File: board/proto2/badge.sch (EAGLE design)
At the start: 59 parts, among them IC1 TLV62569, J1 5051101092

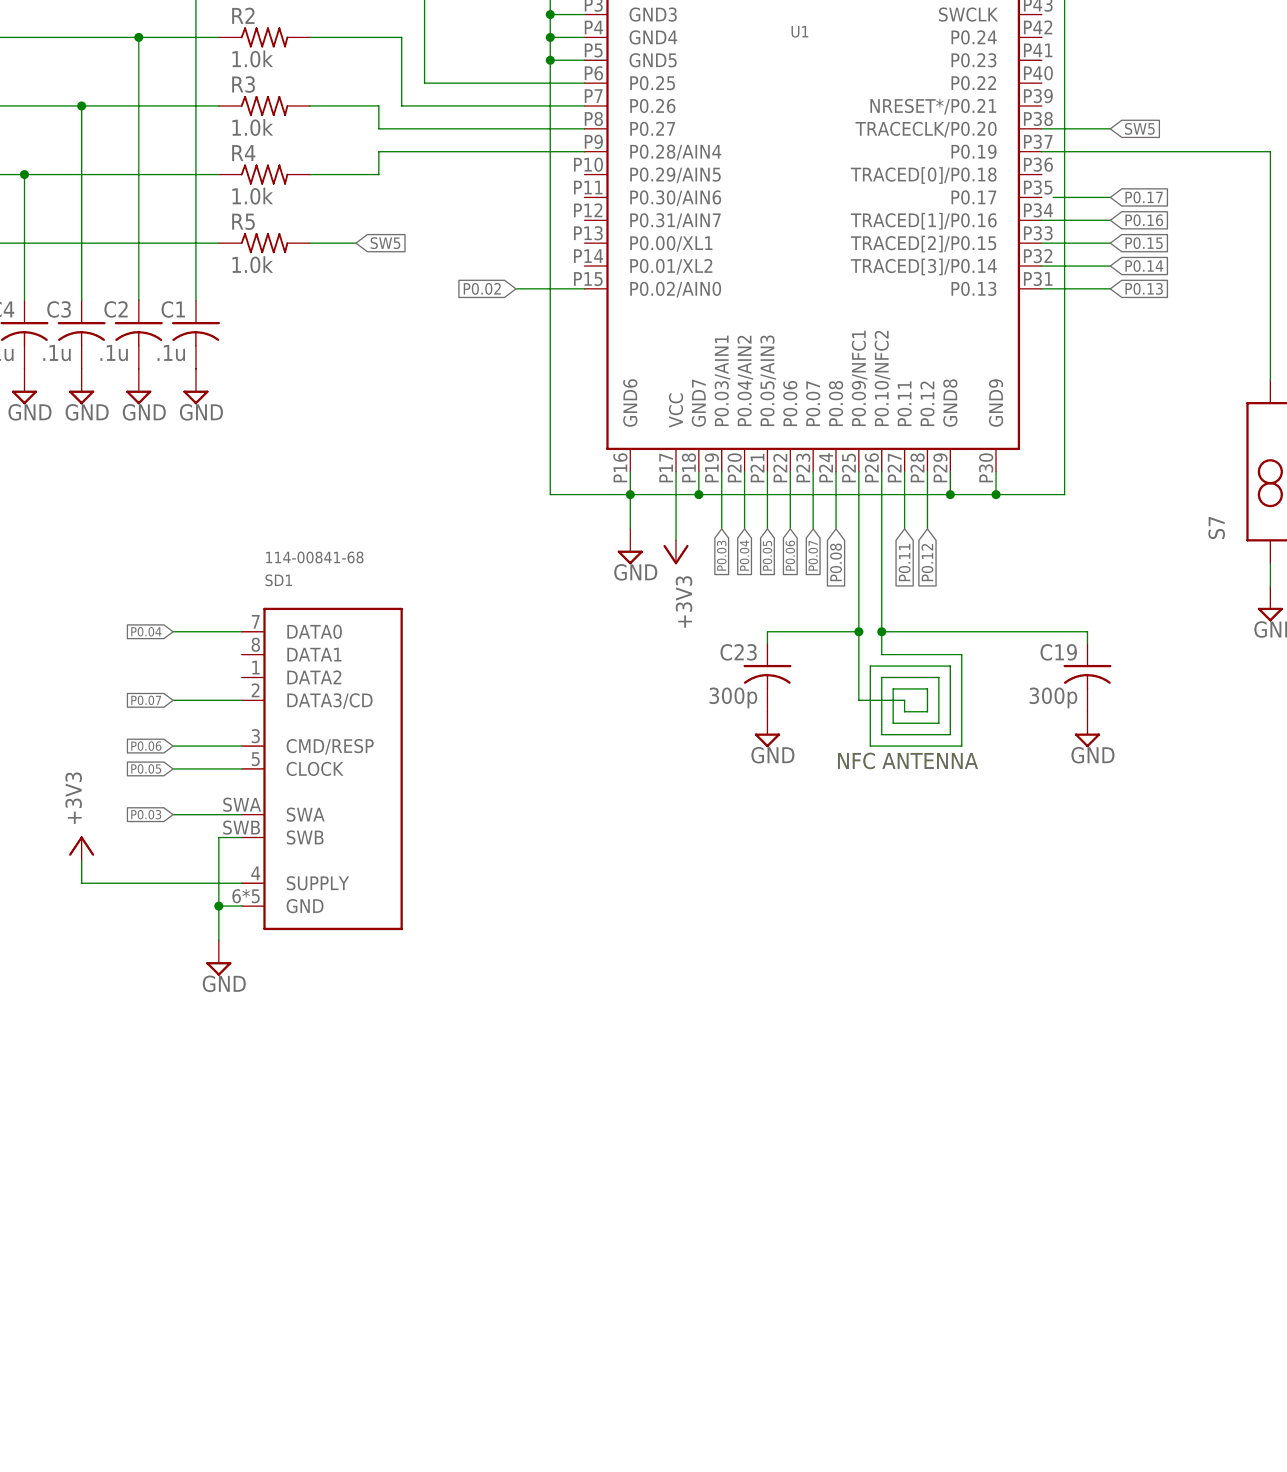
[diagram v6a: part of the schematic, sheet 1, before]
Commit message: added expansion connector to schematic
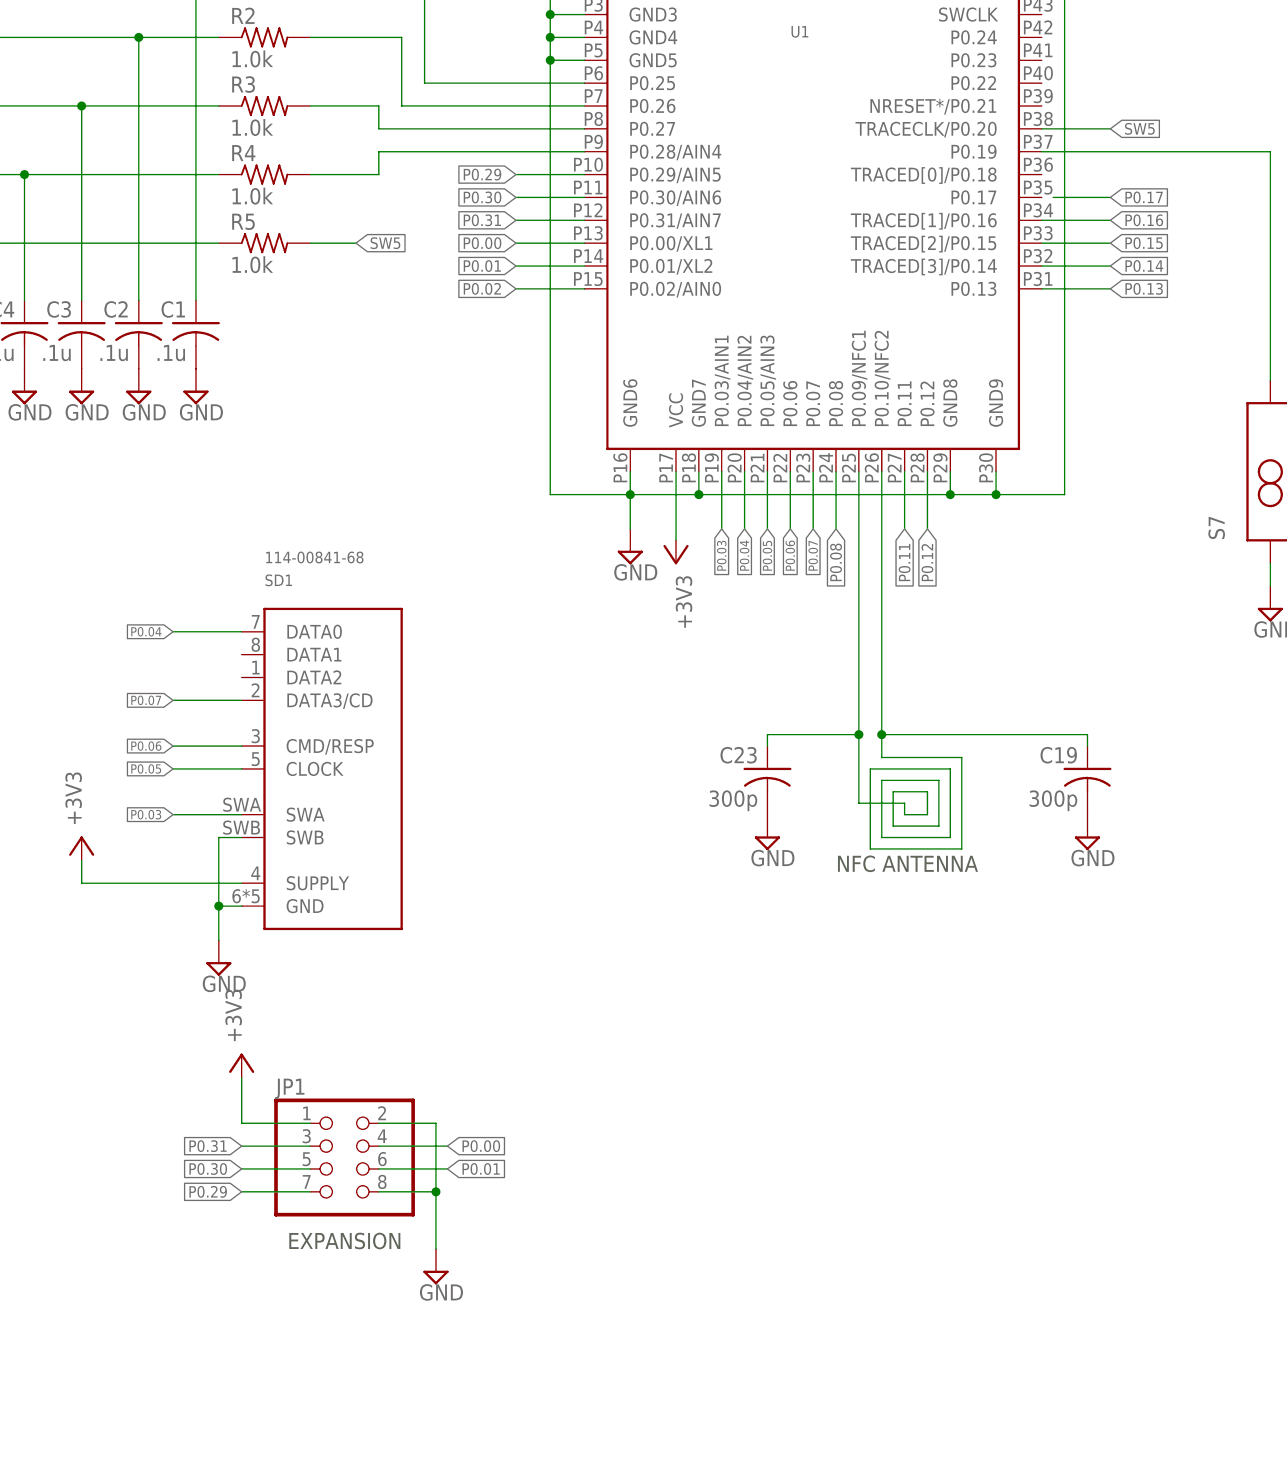
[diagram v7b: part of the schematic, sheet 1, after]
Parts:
- added JP1: (no value), pinhead:PINHD-2X4
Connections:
- new net P0.00: JP1.4, U1.P0.00/XL1
- new net P0.01: JP1.6, U1.P0.01/XL2
- new net P0.29: JP1.7, U1.P0.29/AIN5
- new net P0.30: JP1.5, U1.P0.30/AIN6
- new net P0.31: JP1.3, U1.P0.31/AIN7
- net +3V3: now also JP1.1
- net GND: now also JP1.2, JP1.8
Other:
- note added: "EXPANSION"
- moved on the sheet: C19, C23
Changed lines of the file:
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@@
 <part name="SUPPLY35" library="supply2" deviceset="GND" device=""/>
 <part name="+3V7" library="supply1" deviceset="+3V3" device=""/>
+<part name="JP1" library="pinhead" deviceset="PINHD-2X4" device=""/>
+<part name="+3V8" library="supply1" deviceset="+3V3" device=""/>
+<part name="SUPPLY36" library="supply2" deviceset="GND" device=""/>
 </parts>
 <sheets>
@@
 <text x="86.36" y="168.91" size="1.27" layer="98">ACTION</text>
 <text x="246.38" y="132.08" size="1.778" layer="97" rot="R90">TILT SWITCH</text>
-<text x="190.5" y="106.68" size="1.778" layer="97">NFC ANTENNA</text>
+<text x="190.5" y="95.25" size="1.778" layer="97">NFC ANTENNA</text>
+<text x="129.54" y="53.34" size="1.778" layer="97">EXPANSION</text>
 </plain>
 <instances>
@@
 <instance part="S7" gate="G$1" x="238.76" y="139.7" rot="R90"/>
 <instance part="SUPPLY29" gate="GND" x="238.76" y="124.46"/>
-<instance part="C19" gate="G$1" x="218.44" y="118.11" rot="MR0"/>
-<instance part="C23" gate="G$1" x="182.88" y="118.11" rot="MR0"/>
-<instance part="SUPPLY33" gate="GND" x="182.88" y="110.49"/>
-<instance part="SUPPLY34" gate="GND" x="218.44" y="110.49"/>
+<instance part="C19" gate="G$1" x="218.44" y="106.68" rot="MR0"/>
+<instance part="C23" gate="G$1" x="182.88" y="106.68" rot="MR0"/>
+<instance part="SUPPLY33" gate="GND" x="182.88" y="99.06"/>
+<instance part="SUPPLY34" gate="GND" x="218.44" y="99.06"/>
 <instance part="SD1" gate="G$1" x="134.62" y="106.68"/>
 <instance part="SUPPLY35" gate="GND" x="121.92" y="85.09"/>
@@
 <attribute name="VALUE" x="106.68" y="100.33" size="1.778" layer="96" rot="R90"/>
 </instance>
+<instance part="JP1" gate="A" x="134.62" y="62.23"/>
+<instance part="+3V8" gate="G$1" x="124.46" y="74.93" smashed="yes">
+<attribute name="VALUE" x="124.46" y="76.2" size="1.778" layer="96" rot="R90"/>
+</instance>
+<instance part="SUPPLY36" gate="GND" x="146.05" y="50.8"/>
 </instances>
 <busses>
@@
 <junction x="121.92" y="91.44"/>
 </segment>
+<segment>
+<pinref part="JP1" gate="A" pin="2"/>
+<pinref part="SUPPLY36" gate="GND" pin="GND"/>
+<wire x1="139.7" y1="67.31" x2="146.05" y2="67.31" width="0.1524" layer="91"/>
+<wire x1="146.05" y1="67.31" x2="146.05" y2="59.69" width="0.1524" layer="91"/>
+<pinref part="JP1" gate="A" pin="8"/>
+<wire x1="146.05" y1="59.69" x2="146.05" y2="53.34" width="0.1524" layer="91"/>
+<wire x1="139.7" y1="59.69" x2="146.05" y2="59.69" width="0.1524" layer="91"/>
+<junction x="146.05" y="59.69"/>
+</segment>
 </net>
 <net name="N$10" class="0">
@@
 <wire x1="106.68" y1="93.98" x2="124.46" y2="93.98" width="0.1524" layer="91"/>
 </segment>
+<segment>
+<pinref part="JP1" gate="A" pin="1"/>
+<wire x1="132.08" y1="67.31" x2="124.46" y2="67.31" width="0.1524" layer="91"/>
+<wire x1="124.46" y1="67.31" x2="124.46" y2="72.39" width="0.1524" layer="91"/>
+<pinref part="+3V8" gate="G$1" pin="+3V3"/>
+</segment>
 </net>
 <net name="N$14" class="0">
@@
 <segment>
 <pinref part="U1" gate="G$1" pin="P0.10/NFC2"/>
-<wire x1="195.58" y1="139.7" x2="195.58" y2="121.92" width="0.1524" layer="91"/>
-<wire x1="195.58" y1="121.92" x2="195.58" y2="119.38" width="0.1524" layer="91"/>
-<wire x1="195.58" y1="119.38" x2="204.47" y2="119.38" width="0.1524" layer="91"/>
-<wire x1="204.47" y1="119.38" x2="204.47" y2="109.22" width="0.1524" layer="91"/>
-<wire x1="204.47" y1="109.22" x2="194.31" y2="109.22" width="0.1524" layer="91"/>
-<wire x1="194.31" y1="109.22" x2="194.31" y2="118.11" width="0.1524" layer="91"/>
-<wire x1="194.31" y1="118.11" x2="203.2" y2="118.11" width="0.1524" layer="91"/>
-<wire x1="203.2" y1="118.11" x2="203.2" y2="110.49" width="0.1524" layer="91"/>
-<wire x1="203.2" y1="110.49" x2="195.58" y2="110.49" width="0.1524" layer="91"/>
-<wire x1="195.58" y1="110.49" x2="195.58" y2="116.84" width="0.1524" layer="91"/>
-<wire x1="195.58" y1="116.84" x2="201.93" y2="116.84" width="0.1524" layer="91"/>
-<wire x1="201.93" y1="116.84" x2="201.93" y2="111.76" width="0.1524" layer="91"/>
-<wire x1="201.93" y1="111.76" x2="196.85" y2="111.76" width="0.1524" layer="91"/>
-<wire x1="196.85" y1="111.76" x2="196.85" y2="115.57" width="0.1524" layer="91"/>
-<wire x1="196.85" y1="115.57" x2="200.66" y2="115.57" width="0.1524" layer="91"/>
-<wire x1="200.66" y1="115.57" x2="200.66" y2="113.03" width="0.1524" layer="91"/>
-<wire x1="200.66" y1="113.03" x2="198.12" y2="113.03" width="0.1524" layer="91"/>
-<wire x1="198.12" y1="113.03" x2="198.12" y2="114.3" width="0.1524" layer="91"/>
-<wire x1="198.12" y1="114.3" x2="193.04" y2="114.3" width="0.1524" layer="91"/>
+<wire x1="195.58" y1="139.7" x2="195.58" y2="110.49" width="0.1524" layer="91"/>
+<wire x1="195.58" y1="110.49" x2="195.58" y2="107.95" width="0.1524" layer="91"/>
+<wire x1="195.58" y1="107.95" x2="204.47" y2="107.95" width="0.1524" layer="91"/>
+<wire x1="204.47" y1="107.95" x2="204.47" y2="97.79" width="0.1524" layer="91"/>
+<wire x1="204.47" y1="97.79" x2="194.31" y2="97.79" width="0.1524" layer="91"/>
+<wire x1="194.31" y1="97.79" x2="194.31" y2="106.68" width="0.1524" layer="91"/>
+<wire x1="194.31" y1="106.68" x2="203.2" y2="106.68" width="0.1524" layer="91"/>
+<wire x1="203.2" y1="106.68" x2="203.2" y2="99.06" width="0.1524" layer="91"/>
+<wire x1="203.2" y1="99.06" x2="195.58" y2="99.06" width="0.1524" layer="91"/>
+<wire x1="195.58" y1="99.06" x2="195.58" y2="105.41" width="0.1524" layer="91"/>
+<wire x1="195.58" y1="105.41" x2="201.93" y2="105.41" width="0.1524" layer="91"/>
+<wire x1="201.93" y1="105.41" x2="201.93" y2="100.33" width="0.1524" layer="91"/>
+<wire x1="201.93" y1="100.33" x2="196.85" y2="100.33" width="0.1524" layer="91"/>
+<wire x1="196.85" y1="100.33" x2="196.85" y2="104.14" width="0.1524" layer="91"/>
+<wire x1="196.85" y1="104.14" x2="200.66" y2="104.14" width="0.1524" layer="91"/>
+<wire x1="200.66" y1="104.14" x2="200.66" y2="101.6" width="0.1524" layer="91"/>
+<wire x1="200.66" y1="101.6" x2="198.12" y2="101.6" width="0.1524" layer="91"/>
+<wire x1="198.12" y1="101.6" x2="198.12" y2="102.87" width="0.1524" layer="91"/>
+<wire x1="198.12" y1="102.87" x2="193.04" y2="102.87" width="0.1524" layer="91"/>
 <pinref part="U1" gate="G$1" pin="P0.09/NFC1"/>
-<wire x1="193.04" y1="114.3" x2="193.04" y2="121.92" width="0.1524" layer="91"/>
+<wire x1="193.04" y1="102.87" x2="193.04" y2="110.49" width="0.1524" layer="91"/>
 <pinref part="C23" gate="G$1" pin="1"/>
-<wire x1="193.04" y1="121.92" x2="193.04" y2="139.7" width="0.1524" layer="91"/>
-<wire x1="182.88" y1="120.65" x2="182.88" y2="121.92" width="0.1524" layer="91"/>
-<wire x1="182.88" y1="121.92" x2="193.04" y2="121.92" width="0.1524" layer="91"/>
-<junction x="193.04" y="121.92"/>
+<wire x1="193.04" y1="110.49" x2="193.04" y2="139.7" width="0.1524" layer="91"/>
+<wire x1="182.88" y1="109.22" x2="182.88" y2="110.49" width="0.1524" layer="91"/>
+<wire x1="182.88" y1="110.49" x2="193.04" y2="110.49" width="0.1524" layer="91"/>
+<junction x="193.04" y="110.49"/>
 <pinref part="C19" gate="G$1" pin="1"/>
-<wire x1="195.58" y1="121.92" x2="218.44" y2="121.92" width="0.1524" layer="91"/>
-<wire x1="218.44" y1="121.92" x2="218.44" y2="120.65" width="0.1524" layer="91"/>
-<junction x="195.58" y="121.92"/>
+<wire x1="195.58" y1="110.49" x2="218.44" y2="110.49" width="0.1524" layer="91"/>
+<wire x1="218.44" y1="110.49" x2="218.44" y2="109.22" width="0.1524" layer="91"/>
+<junction x="195.58" y="110.49"/>
 </segment>
 </net>
@@
 </segment>
 </net>
+<net name="P0.31" class="0">
+<segment>
+<pinref part="JP1" gate="A" pin="3"/>
+<wire x1="132.08" y1="64.77" x2="124.46" y2="64.77" width="0.1524" layer="91"/>
+<label x="124.46" y="64.77" size="1.27" layer="93" rot="R180" xref="yes"/>
+</segment>
+<segment>
+<pinref part="U1" gate="G$1" pin="P0.31/AIN7"/>
+<wire x1="162.56" y1="167.64" x2="154.94" y2="167.64" width="0.1524" layer="91"/>
+<label x="154.94" y="167.64" size="1.27" layer="93" rot="R180" xref="yes"/>
+</segment>
+</net>
+<net name="P0.30" class="0">
+<segment>
+<pinref part="JP1" gate="A" pin="5"/>
+<wire x1="132.08" y1="62.23" x2="124.46" y2="62.23" width="0.1524" layer="91"/>
+<label x="124.46" y="62.23" size="1.27" layer="93" rot="R180" xref="yes"/>
+</segment>
+<segment>
+<pinref part="U1" gate="G$1" pin="P0.30/AIN6"/>
+<wire x1="162.56" y1="170.18" x2="154.94" y2="170.18" width="0.1524" layer="91"/>
+<label x="154.94" y="170.18" size="1.27" layer="93" rot="R180" xref="yes"/>
+</segment>
+</net>
+<net name="P0.29" class="0">
+<segment>
+<pinref part="JP1" gate="A" pin="7"/>
+<wire x1="132.08" y1="59.69" x2="124.46" y2="59.69" width="0.1524" layer="91"/>
+<label x="124.46" y="59.69" size="1.27" layer="93" rot="R180" xref="yes"/>
+</segment>
+<segment>
+<pinref part="U1" gate="G$1" pin="P0.29/AIN5"/>
+<wire x1="162.56" y1="172.72" x2="154.94" y2="172.72" width="0.1524" layer="91"/>
+<label x="154.94" y="172.72" size="1.27" layer="93" rot="R180" xref="yes"/>
+</segment>
+</net>
+<net name="P0.00" class="0">
+<segment>
+<pinref part="JP1" gate="A" pin="4"/>
+<wire x1="139.7" y1="64.77" x2="147.32" y2="64.77" width="0.1524" layer="91"/>
+<label x="147.32" y="64.77" size="1.27" layer="93" xref="yes"/>
+</segment>
+<segment>
+<pinref part="U1" gate="G$1" pin="P0.00/XL1"/>
+<wire x1="162.56" y1="165.1" x2="154.94" y2="165.1" width="0.1524" layer="91"/>
+<label x="154.94" y="165.1" size="1.27" layer="93" rot="R180" xref="yes"/>
+</segment>
+</net>
+<net name="P0.01" class="0">
+<segment>
+<pinref part="JP1" gate="A" pin="6"/>
+<wire x1="139.7" y1="62.23" x2="147.32" y2="62.23" width="0.1524" layer="91"/>
+<label x="147.32" y="62.23" size="1.27" layer="93" xref="yes"/>
+</segment>
+<segment>
+<pinref part="U1" gate="G$1" pin="P0.01/XL2"/>
+<wire x1="162.56" y1="162.56" x2="154.94" y2="162.56" width="0.1524" layer="91"/>
+<label x="154.94" y="162.56" size="1.27" layer="93" rot="R180" xref="yes"/>
+</segment>
+</net>
